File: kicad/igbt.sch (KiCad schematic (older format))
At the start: 79 parts, among them U801 SI8660BD, U802 SI8662BD, U803 SN74LVC2G17DBVR, U804 SN74LVC2G17DBVR, U805 SN74LVC2G17DBVR, U806 SN74LVC2G17DBVR, U807 SN74LVC2G17DBVR, U808 SN74LVC2G17DBVR, U809 SN74LVC2G17DBVR, U810 SN74LVC2G17DBVR, U811 SN74LVC2G17DBVR, U812 SN74LVC2G17DBVR, U813 SI8660BD, U814 SI8662BD

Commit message: more bom...
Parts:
- C801, C802, C803, C804, C805, C806, C807, C808, C809, C810, C811, C812, C813, C814, C815, C816, C817, C818, C819, C820, C821, C822, C823, C824: value 10p -> 100pF; Description (none) -> CAP CER 100PF 10V X7R 0603; PartNumber (none) -> 885012206003; digikey (none) -> 732-7922-1-ND
- C825, C826, C833, C834: value 10u -> 10uF; Description (none) -> 10µF ±20% 10V Ceramic Capacitor X5R 0603 (1608 Metric); PartNumber (none) -> GRM188R61A106ME69D; digikey (none) -> 490-10475-1-ND
- C828, C829, C830, C831, C832, C835, C836, C837, C838, C839, C840, C841, C842: value 0.1u -> 0.1uF; Description (none) -> CAP CER 0.1UF 16V X7R 0603; PartNumber (none) -> CC0603KPX7R7BB104; digikey (none) -> 311-1335-1-ND
- R801, R802, R803, R804, R805, R806, R807, R808, R809, R810, R811, R812, R813, R814, R815, R816, R817, R818, R819, R820, R821, R822, R823, R824: value 22e -> 22

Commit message: stackup
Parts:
- C801, C802, C803, C804, C805, C806, C807, C808, C809, C810, C811, C812, C813, C814, C815, C816, C817, C818, C819, C820, C821, C822, C823, C824: price@10 (none) -> 0.02100
- C825, C826, C833, C834: price@10 (none) -> 0.15400
- C828, C829, C830, C831, C832, C835, C836, C837, C838, C839, C840, C841, C842: price@10 (none) -> 0.05800
- U801, U813: Description (none) -> General Purpose Digital Isolator 5000Vrms 6 Channel 150Mbps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; PartNumber (none) -> SI8660BD-B-ISR; digikey (none) -> 336-4786-1-ND; price@10 (none) -> 2.75000
- U802, U814: Description (none) -> General Purpose Digital Isolator 5000Vrms 6 Channel 150Mbps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; PartNumber (none) -> SI8662BD-B-IS; digikey (none) -> 336-2125-5-ND; price@10 (none) -> 2.75000
- U803, U804, U805, U806, U807, U808, U809, U810, U811, U812: Description (none) -> Buffer, Non-Inverting 2 Element 1 Bit per Element Push-Pull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; PartNumber (none) -> SN74LVC2G17DBVR; digikey (none) -> 296-SN74LVC2G17DBVRCT-ND; price@10 (none) -> 0.30200

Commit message: bom copleted
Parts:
- R801, R802, R803, R804, R805, R806, R807, R808, R809, R810, R811, R812, R813, R814, R815, R816, R817, R818, R819, R820, R821, R822, R823, R824: Description (none) -> 22 Ohms ±5% 0.1W, 1/10W Chip Resistor 0603 (1608 Metric) Au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; PartNumber (none) -> CRGCQ0603J22R; digikey (none) -> A130081CT-ND; price@10 (none) -> 0.02100

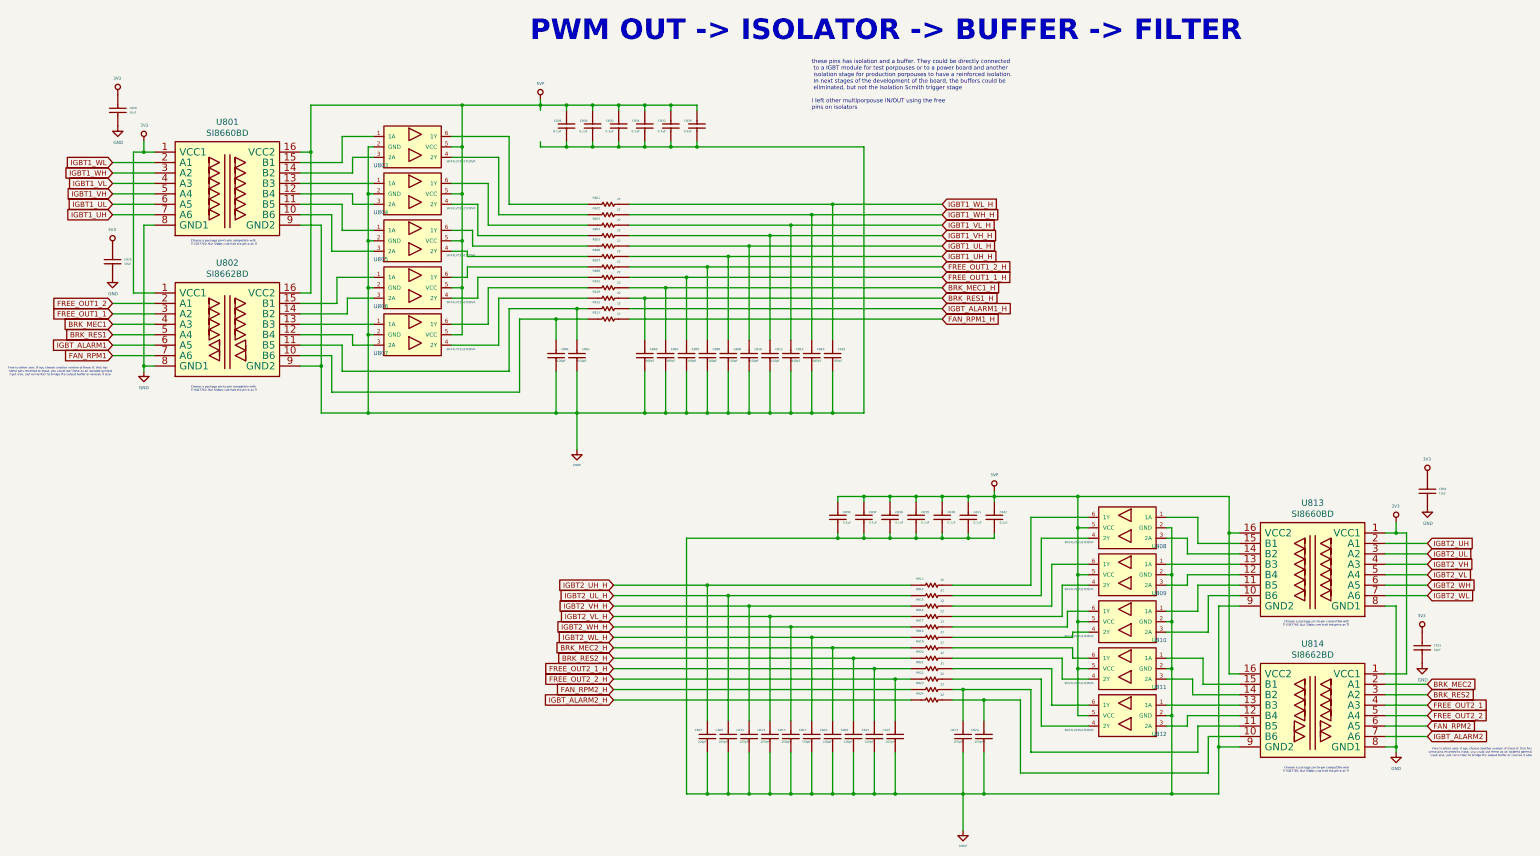
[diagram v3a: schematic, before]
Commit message: changes in footprints
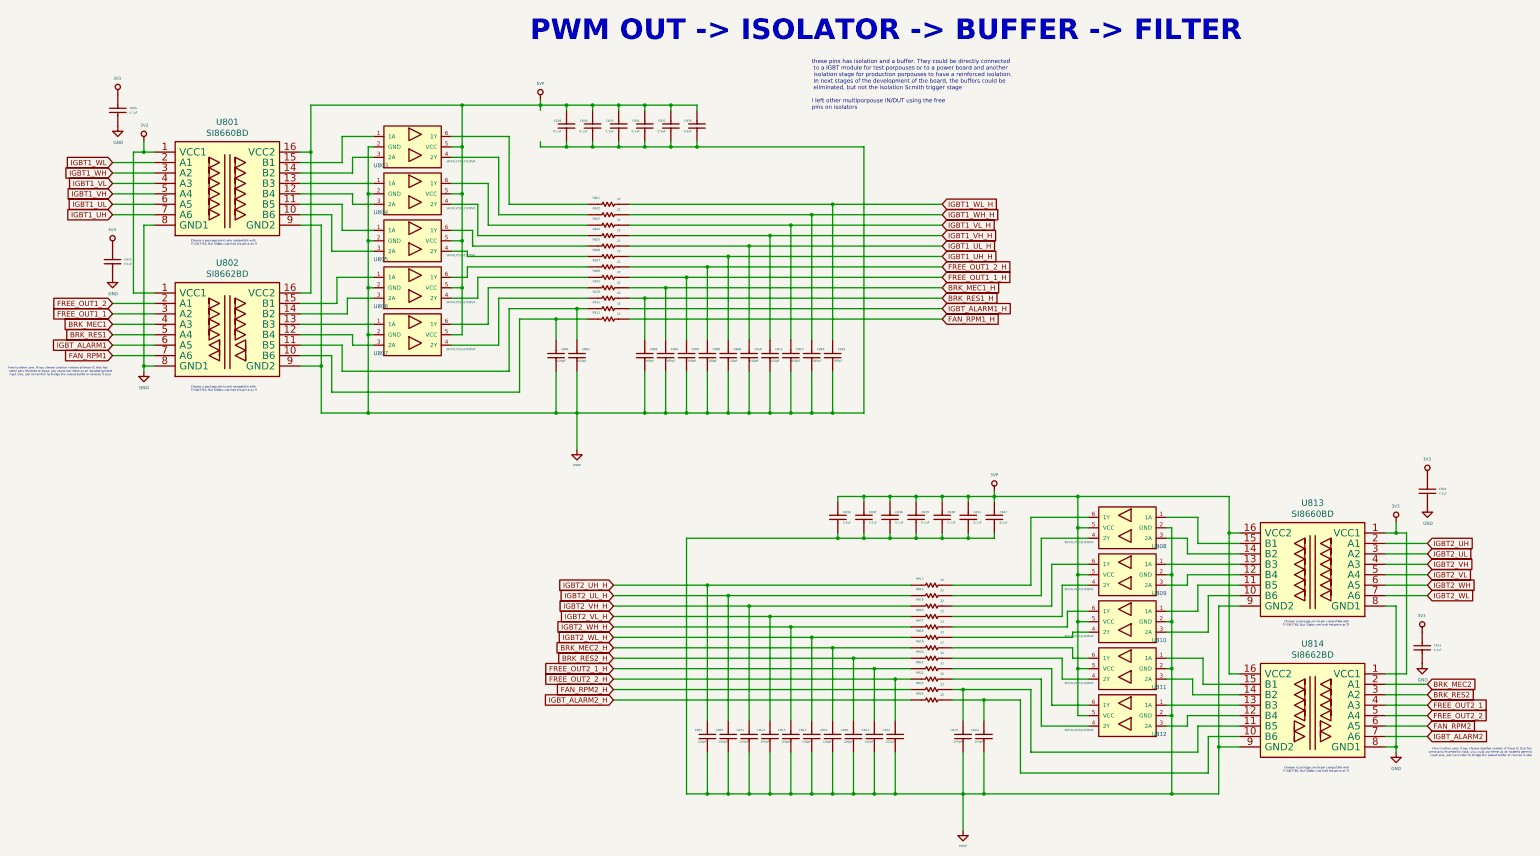
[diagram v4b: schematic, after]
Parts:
- C825, C826, C833, C834: value 10uF -> 0.1uF; Description 10µF ±20% 10V Ceramic Capacitor X5R 0603 (1608 Metric) -> CAP CER 0.1UF 16V X7R 0603; PartNumber GRM188R61A106ME69D -> CC0603KPX7R7BB104; digikey 490-10475-1-ND -> 311-1335-1-ND; price@10 0.15400 -> 0.05800
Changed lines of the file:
@@
 AR Path="/5DDE8C5E/5F157327" Ref="C834"  Part="1"
 F 0 "C834" V 14622 5190 20  0000 R CNN
-F 1 "10uF" V 14579 5190 20  0000 R CNN
+F 1 "0.1uF" V 14579 5190 20  0000 R CNN
 F 2 "servo:C_0603_1608Metric" H 14550 5200 60  0001 C CNN
 F 3 "" H 14550 5300 60  0000 C CNN
-F 4 "10µF ±20% 10V Ceramic Capacitor X5R 0603 (1608 Metric) " H 0   0   50  0001 C CNN "Description"
-F 5 "GRM188R61A106ME69D " H 0   0   50  0001 C CNN "PartNumber"
-F 6 "490-10475-1-ND" H 0   0   50  0001 C CNN "digikey"
-F 7 "0.15400" H 0   0   50  0001 C CNN "price@10"
+F 4 "CAP CER 0.1UF 16V X7R 0603 " H 0   0   50  0001 C CNN "Description"
+F 5 "CC0603KPX7R7BB104" H 0   0   50  0001 C CNN "PartNumber"
+F 6 "311-1335-1-ND" H 0   0   50  0001 C CNN "digikey"
+F 7 "0.05800" H 0   0   50  0001 C CNN "price@10"
 	1    14550 5300
 	0    -1   -1   0
@@
 AR Path="/5DDE8C5E/5F1795FC" Ref="C833"  Part="1"
 F 0 "C833" V 14572 6690 20  0000 R CNN
-F 1 "10uF" V 14529 6690 20  0000 R CNN
+F 1 "0.1uF" V 14529 6690 20  0000 R CNN
 F 2 "servo:C_0603_1608Metric" H 14500 6700 60  0001 C CNN
 F 3 "" H 14500 6800 60  0000 C CNN
-F 4 "10µF ±20% 10V Ceramic Capacitor X5R 0603 (1608 Metric) " H 0   0   50  0001 C CNN "Description"
-F 5 "GRM188R61A106ME69D " H 0   0   50  0001 C CNN "PartNumber"
-F 6 "490-10475-1-ND" H 0   0   50  0001 C CNN "digikey"
-F 7 "0.15400" H 0   0   50  0001 C CNN "price@10"
+F 4 "CAP CER 0.1UF 16V X7R 0603 " H 0   0   50  0001 C CNN "Description"
+F 5 "CC0603KPX7R7BB104" H 0   0   50  0001 C CNN "PartNumber"
+F 6 "311-1335-1-ND" H 0   0   50  0001 C CNN "digikey"
+F 7 "0.05800" H 0   0   50  0001 C CNN "price@10"
 	1    14500 6800
 	0    -1   -1   0
@@
 AR Path="/5DDE8C5E/5F19B896" Ref="C826"  Part="1"
 F 0 "C826" V 2072 1540 20  0000 R CNN
-F 1 "10uF" V 2029 1540 20  0000 R CNN
+F 1 "0.1uF" V 2029 1540 20  0000 R CNN
 F 2 "servo:C_0603_1608Metric" H 2000 1550 60  0001 C CNN
 F 3 "" H 2000 1650 60  0000 C CNN
-F 4 "10µF ±20% 10V Ceramic Capacitor X5R 0603 (1608 Metric) " H 0   0   50  0001 C CNN "Description"
-F 5 "GRM188R61A106ME69D " H 0   0   50  0001 C CNN "PartNumber"
-F 6 "490-10475-1-ND" H 0   0   50  0001 C CNN "digikey"
-F 7 "0.15400" H 0   0   50  0001 C CNN "price@10"
+F 4 "CAP CER 0.1UF 16V X7R 0603 " H 0   0   50  0001 C CNN "Description"
+F 5 "CC0603KPX7R7BB104" H 0   0   50  0001 C CNN "PartNumber"
+F 6 "311-1335-1-ND" H 0   0   50  0001 C CNN "digikey"
+F 7 "0.05800" H 0   0   50  0001 C CNN "price@10"
 	1    2000 1650
 	0    -1   -1   0
@@
 AR Path="/5DDE8C5E/5F1BD8B6" Ref="C825"  Part="1"
 F 0 "C825" V 2022 2990 20  0000 R CNN
-F 1 "10uF" V 1979 2990 20  0000 R CNN
+F 1 "0.1uF" V 1979 2990 20  0000 R CNN
 F 2 "servo:C_0603_1608Metric" H 1950 3000 60  0001 C CNN
 F 3 "" H 1950 3100 60  0000 C CNN
-F 4 "10µF ±20% 10V Ceramic Capacitor X5R 0603 (1608 Metric) " H 0   0   50  0001 C CNN "Description"
-F 5 "GRM188R61A106ME69D " H 0   0   50  0001 C CNN "PartNumber"
-F 6 "490-10475-1-ND" H 0   0   50  0001 C CNN "digikey"
-F 7 "0.15400" H 0   0   50  0001 C CNN "price@10"
+F 4 "CAP CER 0.1UF 16V X7R 0603 " H 0   0   50  0001 C CNN "Description"
+F 5 "CC0603KPX7R7BB104" H 0   0   50  0001 C CNN "PartNumber"
+F 6 "311-1335-1-ND" H 0   0   50  0001 C CNN "digikey"
+F 7 "0.05800" H 0   0   50  0001 C CNN "price@10"
 	1    1950 3100
 	0    -1   -1   0

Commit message: gerbers + pnp + bom ready
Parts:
- C801, C802, C803, C804, C805, C806, C807, C808, C809, C810, C811, C812, C813, C814, C815, C816, C817, C818, C819, C820, C821, C822, C823, C824, C825, C826, C828, C829, C830, C831, C832, C833, C834, C835, C836, C837, C838, C839, C840, C841, C842, R801, R802, R803, R804, R805, R806, R807, R808, R809, R810, R811, R812, R813, R814, R815, R816, R817, R818, R819, R820, R821, R822, R823, R824: bom_1 (none) -> 1; bom_2 (none) -> 1; bom_3 (none) -> 1
- U801, U802, U803, U804, U805, U806, U807, U808, U809, U810, U811, U812, U813, U814: bom_2 (none) -> 1; bom_3 (none) -> 1

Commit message: some details on gerbers, now released
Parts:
- U801, U802, U803, U804, U805, U806, U807, U808, U809, U810, U811, U812, U813, U814: bom_1 (none) -> 0
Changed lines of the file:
@@
 F 6 " 336-4786-1-ND" H 0   0   50  0001 C CNN "digikey"
 F 7 "2.75000" H 0   0   50  0001 C CNN "price@10"
-F 8 "" H 0   0   50  0001 C CNN "bom_1"
+F 8 "0" H 0   0   50  0001 C CNN "bom_1"
 F 9 "1" H 0   0   50  0001 C CNN "bom_2"
 F 10 "1" H 0   0   50  0001 C CNN "bom_3"
@@
 F 6 "336-2125-5-ND " H 0   0   50  0001 C CNN "digikey"
 F 7 "2.75000" H 0   0   50  0001 C CNN "price@10"
-F 8 "" H 0   0   50  0001 C CNN "bom_1"
+F 8 "0" H 0   0   50  0001 C CNN "bom_1"
 F 9 "1" H 0   0   50  0001 C CNN "bom_2"
 F 10 "1" H 0   0   50  0001 C CNN "bom_3"
@@
 F 6 " 296-SN74LVC2G17DBVRCT-ND " H 0   0   50  0001 C CNN "digikey"
 F 7 "0.30200" H 0   0   50  0001 C CNN "price@10"
-F 8 "" H 0   0   50  0001 C CNN "bom_1"
+F 8 "0" H 0   0   50  0001 C CNN "bom_1"
 F 9 "1" H 0   0   50  0001 C CNN "bom_2"
 F 10 "1" H 0   0   50  0001 C CNN "bom_3"
@@
 F 6 " 296-SN74LVC2G17DBVRCT-ND " H 0   0   50  0001 C CNN "digikey"
 F 7 "0.30200" H 0   0   50  0001 C CNN "price@10"
-F 8 "" H 0   0   50  0001 C CNN "bom_1"
+F 8 "0" H 0   0   50  0001 C CNN "bom_1"
 F 9 "1" H 0   0   50  0001 C CNN "bom_2"
 F 10 "1" H 0   0   50  0001 C CNN "bom_3"
@@
 F 6 " 296-SN74LVC2G17DBVRCT-ND " H 0   0   50  0001 C CNN "digikey"
 F 7 "0.30200" H 0   0   50  0001 C CNN "price@10"
-F 8 "" H 0   0   50  0001 C CNN "bom_1"
+F 8 "0" H 0   0   50  0001 C CNN "bom_1"
 F 9 "1" H 0   0   50  0001 C CNN "bom_2"
 F 10 "1" H 0   0   50  0001 C CNN "bom_3"
@@
 F 6 " 296-SN74LVC2G17DBVRCT-ND " H 0   0   50  0001 C CNN "digikey"
 F 7 "0.30200" H 0   0   50  0001 C CNN "price@10"
-F 8 "" H 0   0   50  0001 C CNN "bom_1"
+F 8 "0" H 0   0   50  0001 C CNN "bom_1"
 F 9 "1" H 0   0   50  0001 C CNN "bom_2"
 F 10 "1" H 0   0   50  0001 C CNN "bom_3"
@@
 F 6 " 336-4786-1-ND" H 0   0   50  0001 C CNN "digikey"
 F 7 "2.75000" H 0   0   50  0001 C CNN "price@10"
-F 8 "" H 0   0   50  0001 C CNN "bom_1"
+F 8 "0" H 0   0   50  0001 C CNN "bom_1"
 F 9 "1" H 0   0   50  0001 C CNN "bom_2"
 F 10 "1" H 0   0   50  0001 C CNN "bom_3"
@@
 F 6 "336-2125-5-ND " H 0   0   50  0001 C CNN "digikey"
 F 7 "2.75000" H 0   0   50  0001 C CNN "price@10"
-F 8 "" H 0   0   50  0001 C CNN "bom_1"
+F 8 "0" H 0   0   50  0001 C CNN "bom_1"
 F 9 "1" H 0   0   50  0001 C CNN "bom_2"
 F 10 "1" H 0   0   50  0001 C CNN "bom_3"
@@
 F 6 " 296-SN74LVC2G17DBVRCT-ND " H 0   0   50  0001 C CNN "digikey"
 F 7 "0.30200" H 0   0   50  0001 C CNN "price@10"
-F 8 "" H 0   0   50  0001 C CNN "bom_1"
+F 8 "0" H 0   0   50  0001 C CNN "bom_1"
 F 9 "1" H 0   0   50  0001 C CNN "bom_2"
 F 10 "1" H 0   0   50  0001 C CNN "bom_3"
@@
 F 6 " 296-SN74LVC2G17DBVRCT-ND " H 0   0   50  0001 C CNN "digikey"
 F 7 "0.30200" H 0   0   50  0001 C CNN "price@10"
-F 8 "" H 0   0   50  0001 C CNN "bom_1"
+F 8 "0" H 0   0   50  0001 C CNN "bom_1"
 F 9 "1" H 0   0   50  0001 C CNN "bom_2"
 F 10 "1" H 0   0   50  0001 C CNN "bom_3"
@@
 F 6 " 296-SN74LVC2G17DBVRCT-ND " H 0   0   50  0001 C CNN "digikey"
 F 7 "0.30200" H 0   0   50  0001 C CNN "price@10"
-F 8 "" H 0   0   50  0001 C CNN "bom_1"
+F 8 "0" H 0   0   50  0001 C CNN "bom_1"
 F 9 "1" H 0   0   50  0001 C CNN "bom_2"
 F 10 "1" H 0   0   50  0001 C CNN "bom_3"
@@
 F 6 " 296-SN74LVC2G17DBVRCT-ND " H 0   0   50  0001 C CNN "digikey"
 F 7 "0.30200" H 0   0   50  0001 C CNN "price@10"
-F 8 "" H 0   0   50  0001 C CNN "bom_1"
+F 8 "0" H 0   0   50  0001 C CNN "bom_1"
 F 9 "1" H 0   0   50  0001 C CNN "bom_2"
 F 10 "1" H 0   0   50  0001 C CNN "bom_3"
@@
 F 6 " 296-SN74LVC2G17DBVRCT-ND " H 0   0   50  0001 C CNN "digikey"
 F 7 "0.30200" H 0   0   50  0001 C CNN "price@10"
-F 8 "" H 0   0   50  0001 C CNN "bom_1"
+F 8 "0" H 0   0   50  0001 C CNN "bom_1"
 F 9 "1" H 0   0   50  0001 C CNN "bom_2"
 F 10 "1" H 0   0   50  0001 C CNN "bom_3"
@@
 F 6 " 296-SN74LVC2G17DBVRCT-ND " H 0   0   50  0001 C CNN "digikey"
 F 7 "0.30200" H 0   0   50  0001 C CNN "price@10"
-F 8 "" H 0   0   50  0001 C CNN "bom_1"
-F 9 "1" H 0   0   50  0001 C CNN "bom_2"
-F 10 "1" H 0   0   50  0001 C CNN "bom_3"
+F 8 "0" H 0   0   50  0001 C CNN "bom_1"
+F 9 "1" H 0   0   50  0001 C CNN "bom_2"
+F 10 "1" H 0   0   50  0001 C CNN "bom_3"
